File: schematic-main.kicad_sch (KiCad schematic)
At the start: 47 parts, among them J1 Conn_01x02_Socket, J4 Conn_01x02_Pin, P1 USB_C_Plug_USB2.0, SW2 SW_Push, U1 STM32F042F6Px, U2 MQ-8, U3 SN65HVD232, U5 USBLC6-2P6, U6 ESP32-S3FN8, Y1 Crystal_GND24

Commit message: Format main schematic and add I/O section
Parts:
- removed C13: 10n, symbol Device:C
- removed C14, C15: 1u, symbol Device:C
- removed FB1: 120R@100 MHz, symbol Device:FerriteBead
- removed U1: STM32F042F6Px, Package_SO:TSSOP-20_4.4x6.5mm_P0.65mm, symbol MCU_ST_STM32F0:STM32F042F6Px
- added R23: 10k, symbol Device:R
- added SW1: SW_Push, symbol Switch:SW_Push
- C2: value 10u -> 1u
- C28, C33: value C -> 1u
- C29: value C -> 10n
- C30, C31, C34: value C -> 100n
- C32: value C -> 10u
- C4, C5: value 20p -> 12p
- L3: value L -> 2n
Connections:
- net +3.3V: now also D6.1 (K), R23.2; no longer C2.1
- net CAN_RX: now also U6.44 (MTCK/JTAG/GPIO39)
- net CAN_TX: now also U6.45 (MTDO/JTAG/GPIO40)
- net GND: now also U6.57 (GND), SW1.1
- net RESET: now also C2.1, R23.1, SW1.2
- net BOOT: now reaches U6.5 (GPIO0/BOOT)
- no-connect marks 7 -> 3
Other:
- added sheet IO (schematc-io.kicad_sch)
- note added: "Boot button"
- note added: "C_{x} = (C_{load} - C_{stray}) * 2 = = (8 pF - 2 pF) * 2 = 12 pF"
- note added: "Power section"
- note added: "TODO: Add diode's pinout Update component numeration"
- note added: "USB-C (programming and debugging)"
- note removed: "C12 = (C_load - C_stray) x 2 = (8 + 2) * 2"
- note removed: "I_{VDD_max}: 120 mA P_{max}: 265 mW"
- note removed: "TODO: ESP32 vs STM32 ESP32 SoC vs module Check crystal osc values Add VDD pins' filters USB C? JTAG+UART Update component numeration Annotate document"
- note removed: "TODO: We may use 4 pin connector with CAN"
- moved on the sheet: C27, C28, C29, C30, C31, C32, C33, C34, C35, C4, C5, C6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

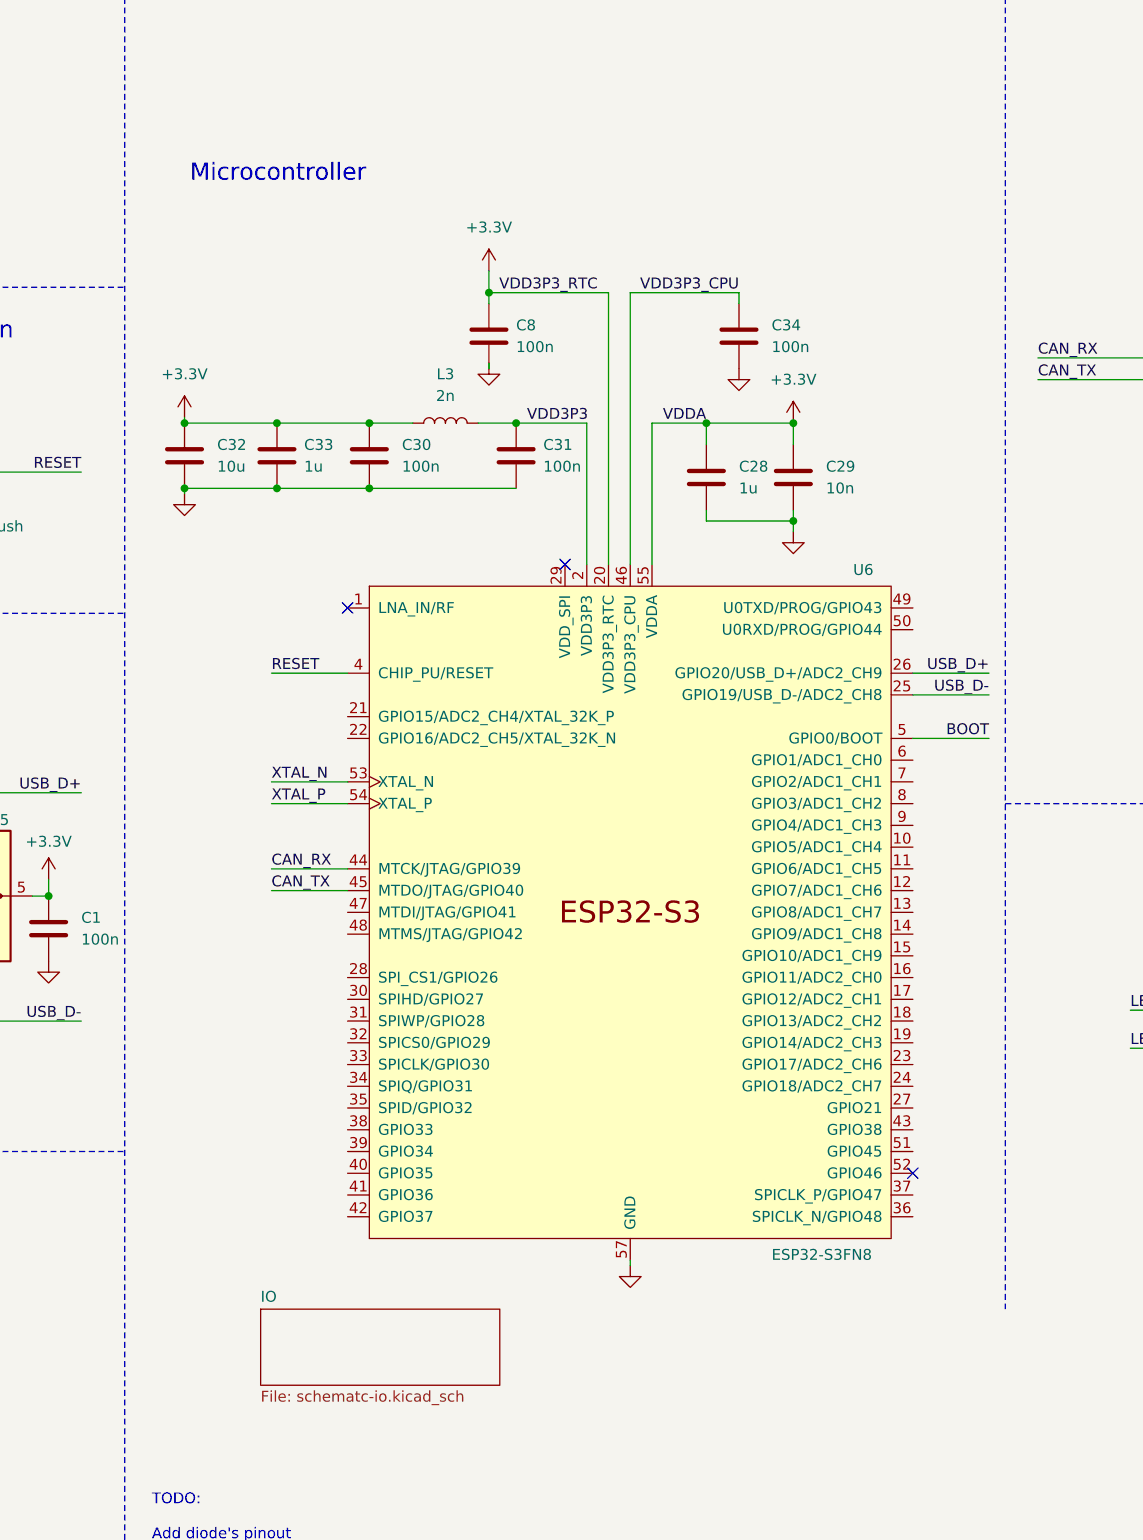
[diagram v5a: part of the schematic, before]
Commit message: Add optocouplers and move ESP to I/O section
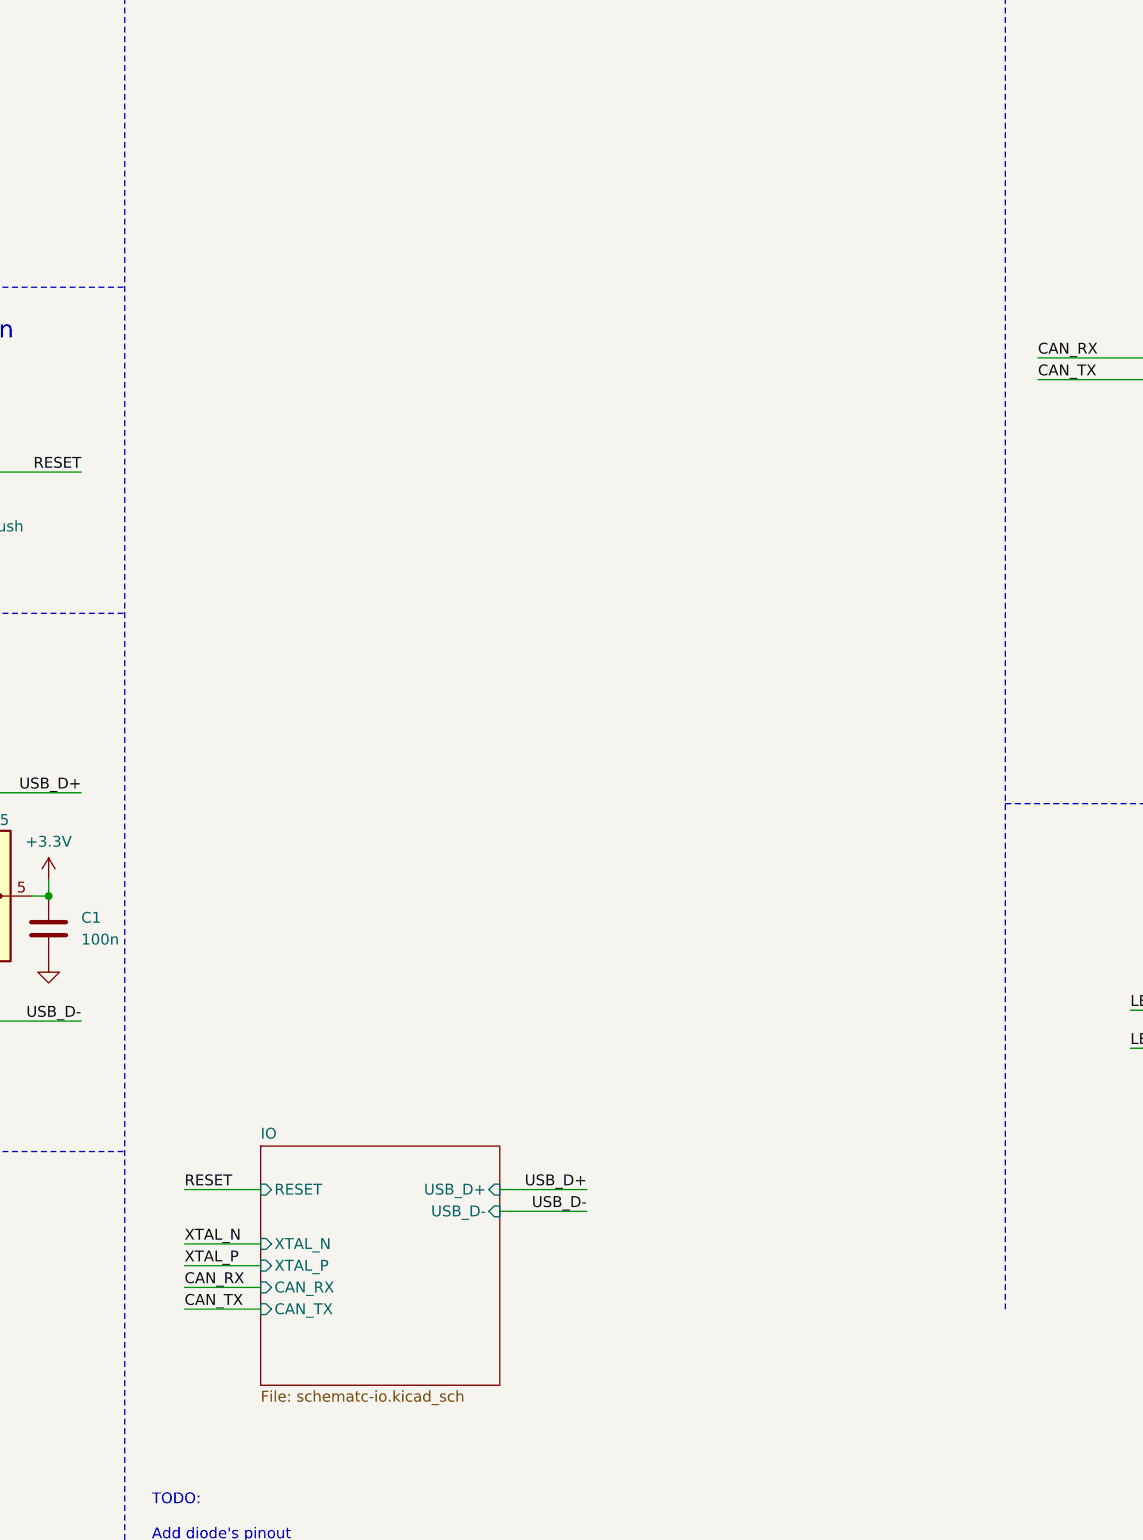
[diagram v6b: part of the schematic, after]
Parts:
- removed C28, C33: 1u, symbol Device:C
- removed C29: 10n, symbol Device:C
- removed C30, C31, C34, C8: 100n, symbol Device:C
- removed C32: 10u, symbol Device:C
- removed L3: 2n, symbol Device:L
- removed U6: ESP32-S3FN8, Package_DFN_QFN:QFN-56-1EP_7x7mm_P0.4mm_EP5.6x5.6mm, symbol PCM_Espressif:ESP32-S3
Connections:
- no-connect marks 3 -> 0
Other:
- sheet IO ports: added CAN_RX, CAN_TX, RESET, USB_D+, USB_D-, XTAL_N, XTAL_P; removed none
- note removed: "Microcontroller"

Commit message: Redesign schematic structure using hierarchical sheets
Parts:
- removed C1, C6, C7: 100n, symbol Device:C
- removed C2, C35: 1u, symbol Device:C
- removed C27: 4n7, symbol Device:C
- removed C4, C5: 12p, symbol Device:C
- removed D2, D3, D4: LED, symbol Device:LED
- removed D5: SP0502BAJT, Package_TO_SOT_SMD:SOT-323_SC-70, symbol Power_Protection:SP0502BAJT
- removed D6: D, symbol Device:D
- removed J1: Conn_01x02_Socket, symbol Connector:Conn_01x02_Socket
- removed R17, R18: 60, symbol Device:R
- removed R19, R22: 5k1, symbol Device:R
- removed R20, R21: 0, symbol Device:R
- removed R23, R5: 10k, symbol Device:R
- removed SW1, SW2: SW_Push, symbol Switch:SW_Push
- removed U2: MQ-8, Sensor:MQ-6, symbol Sensor_Gas:MQ-6
- removed U3: SN65HVD232, Package_SO:SOIC-8_3.9x4.9mm_P1.27mm, symbol Interface_CAN_LIN:SN65HVD232
- removed U5: USBLC6-2P6, Package_TO_SOT_SMD:SOT-666, symbol Power_Protection:USBLC6-2P6
- removed Y1: Crystal_GND24, symbol Device:Crystal_GND24
- added J1, J2, J3: Conn_01x02_Pin, symbol Connector:Conn_01x02_Pin
- R1: value 10k -> 0
- R2: value 1k -> 0
- R3, R4: value 1k -> 5k1
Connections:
- net SENSOR_ADC is gone; now on an unnamed net: R1.1
- net GND: now also J1.2 (Pin_2); no longer J4.2 (Pin_2), R1.2, R2.2
- net Power /Vin: now also J1.1 (Pin_1); no longer J4.1 (Pin_1)
- net at P1.B5 (VCONN): now also R3.1
- net MCU/USB_VBUS: now reaches P1.A4 (VBUS), P1.A9 (VBUS), P1.B4 (VBUS), P1.B9 (VBUS)
- net at R2.1: now also P1.A6 (D+)
- net at P1.A5 (CC): now also R4.1
- new net IO/5V_MOTOR: J3.1 (Pin_1)
- new net IO/CANH: J2.1 (Pin_1)
- new net IO/CANL: J2.2 (Pin_2)
- new net IO/GND_MOTOR: J3.2 (Pin_2)
- new net IO/MOTOR_ON_OFF: J4.2 (Pin_2)
- new net IO/PWM_OUT: J4.1 (Pin_1)
- new net MCU/USB_D+: R2.2
- new net MCU/USB_D-: R1.2
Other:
- added sheet MCU (schematic-mcu.kicad_sch)
- sheet IO ports: added 3.3V, 5V_MOTOR, CANH, CANL, GND, GND_MOTOR, LED_CAN_STATUS, LED_MCU_STATUS, MOTOR_ON_OFF, MOTOR_ON_OFF_MCU, PWM_MCU, PWM_OUT; removed RESET, USB_D+, USB_D-, XTAL_N, XTAL_P
- sheet Power  ports: added GND; removed +5V
- note removed: "Boot button"
- note removed: "CAN Transceiver"
- note removed: "C_{x} = (C_{load} - C_{stray}) * 2 = = (8 pF - 2 pF) * 2 = 12 pF"
- note removed: "Crystal oscillator"
- note removed: "Hydrogen sensor"
- note removed: "I_{max}: 250 mA P_{max}: 800 mW"
- note removed: "Power section"
- note removed: "Reset button"
- note removed: "Signal diodes"
- note removed: "TODO Protect USB reverse-polarity Ensure MCU receive 3.3 V from USB-C"
- note removed: "TODO: Add diode's pinout Update component numeration"
- note removed: "Termination node (resistors and capacitor) may be omitted during assembly if not required."
- note removed: "USB-C (programming and debugging)"
- title: Hydrogen sensor -> Motor driver unit

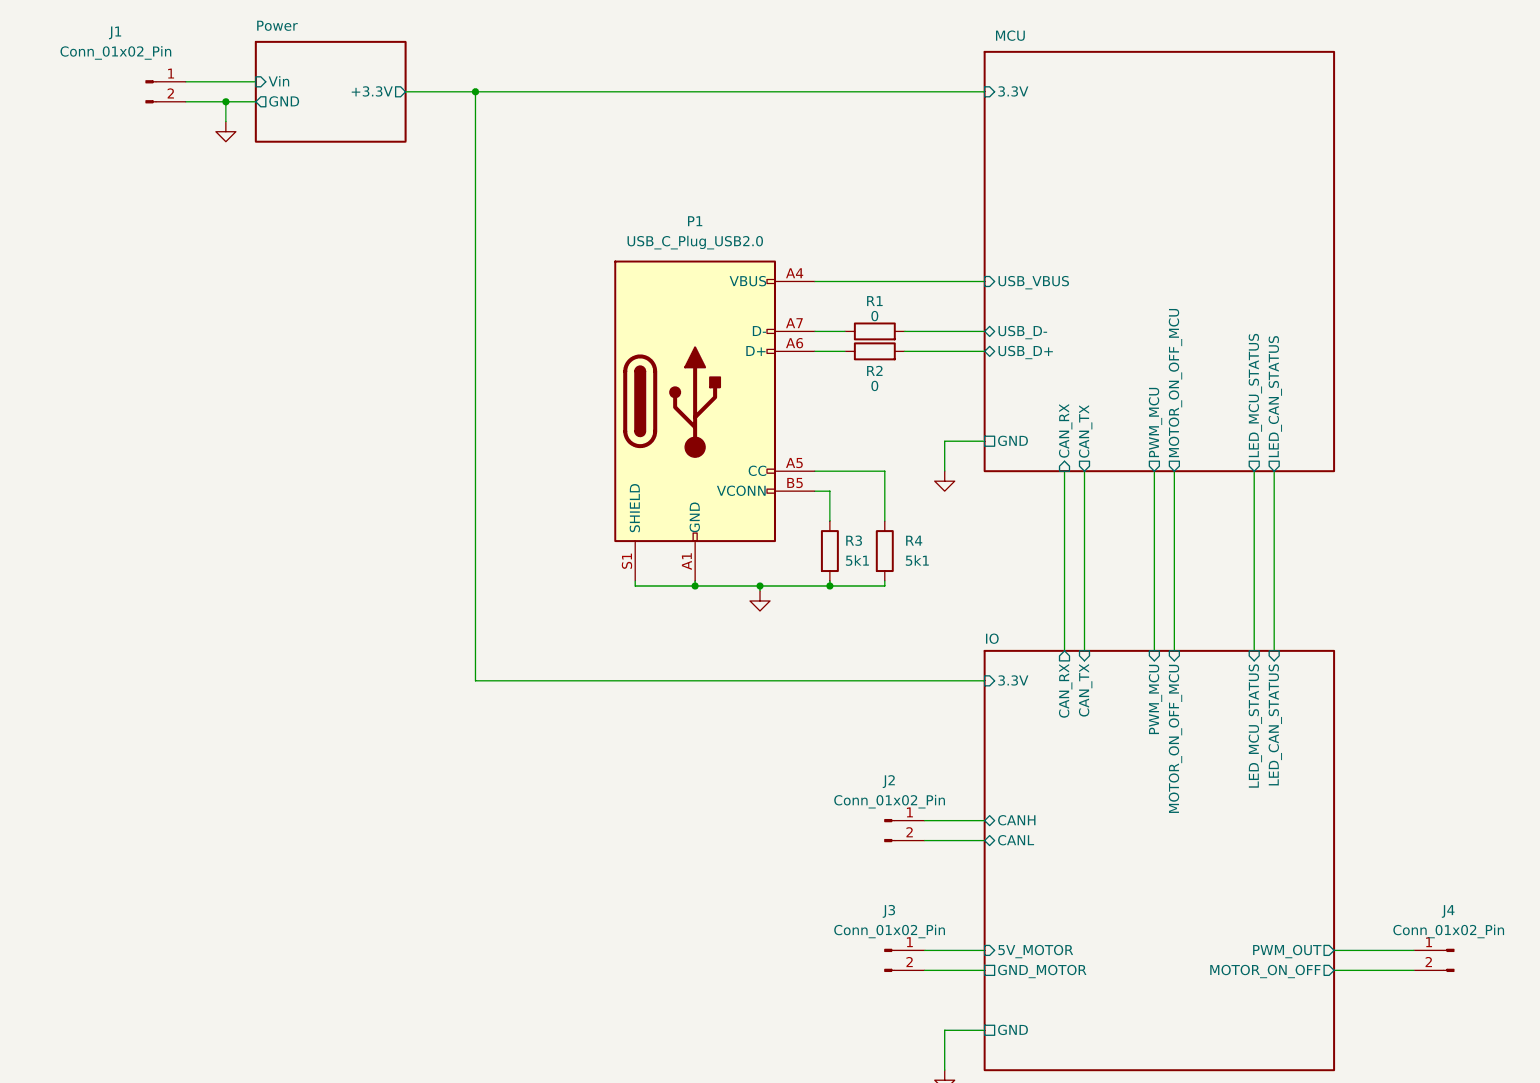
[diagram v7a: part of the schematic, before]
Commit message: Fix most issues with found after ERC
Grid size, unconnected ping, PWR_FLAGs
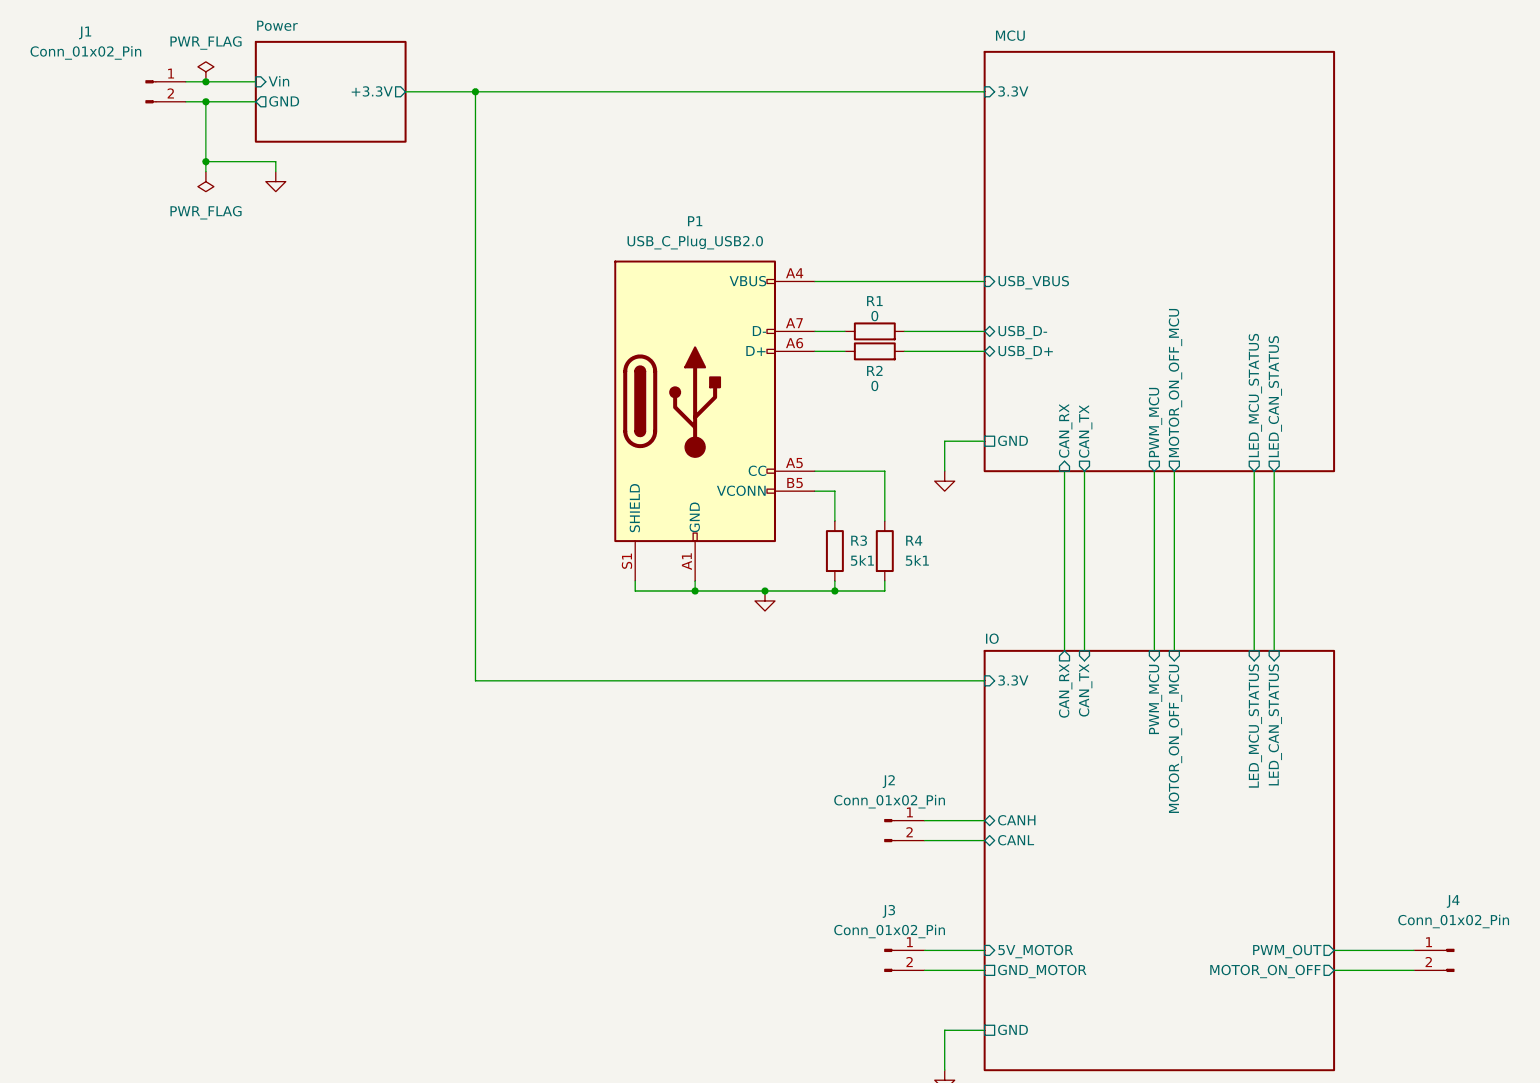
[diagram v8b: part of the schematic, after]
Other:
- moved on the sheet: R3
